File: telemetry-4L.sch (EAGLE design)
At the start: 65 parts, among them SW1 MF-SW-TACT-4.2MM, SW2 SWITCH_SPDT, U1 ATSAMD21G18A-MUT, U2 SPX3819M5-L-3-0, U3 MCP73831T-2ACI/OT, U4 DMG6968U, U5 SIM868, U6 BMP280, U7 MPU-9250, X1 S2B-PH-SM4-TB(LF)(SN)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

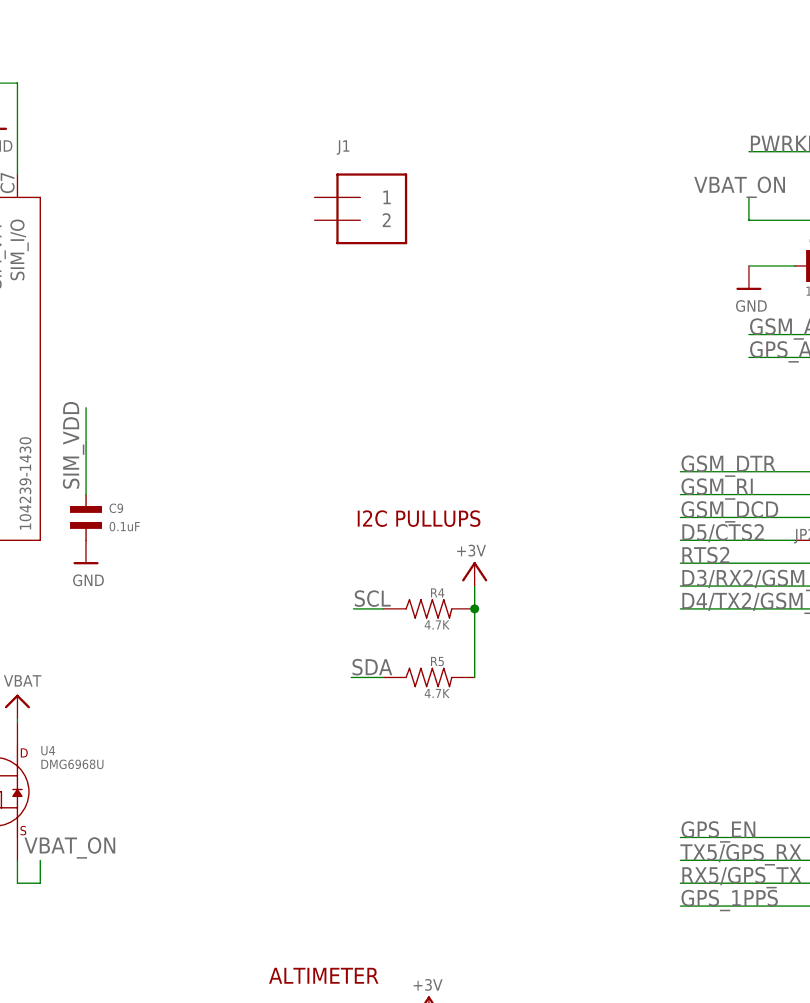
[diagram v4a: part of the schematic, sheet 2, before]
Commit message: Added a second JP2 socket for servo output
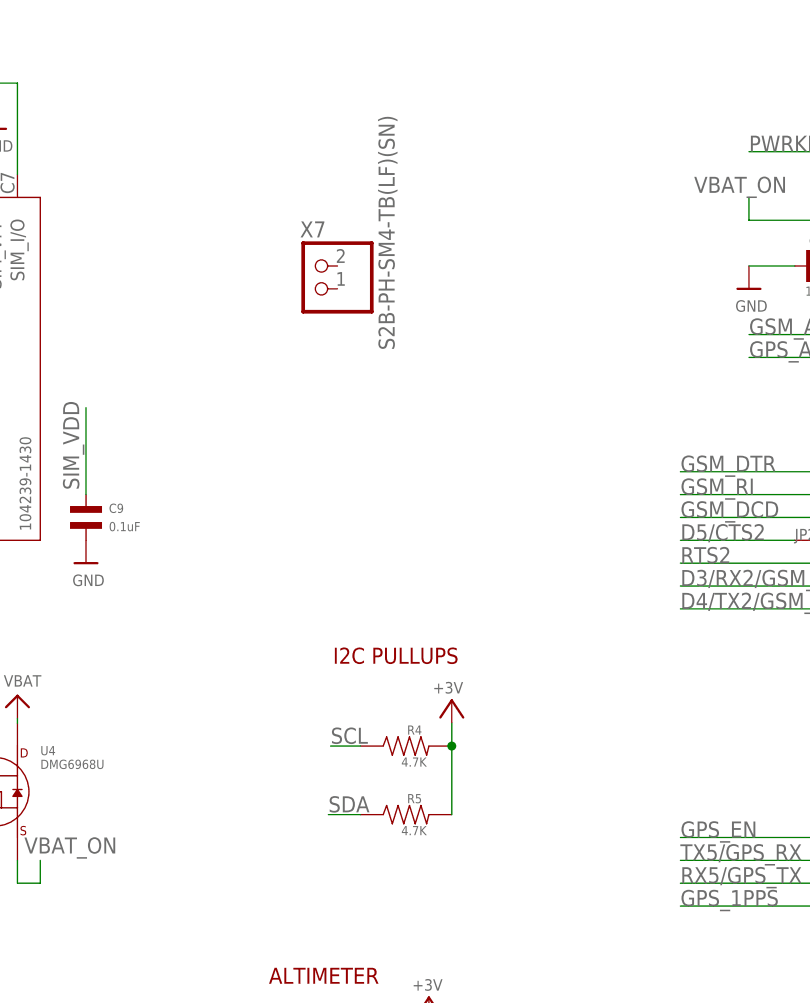
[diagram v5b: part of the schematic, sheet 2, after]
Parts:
- removed J1: (no value), microbuilder:TERMBLOCK_1X2
- added X7: S2B-PH-SM4-TB(LF)(SN), microbuilder:CON_JST_PH_2PIN
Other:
- moved on the sheet: R4, R5
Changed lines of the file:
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@@
 <part name="U$25" library="microbuilder" deviceset="GND" device=""/>
 <part name="U$26" library="microbuilder" deviceset="GND" device=""/>
-<part name="J1" library="microbuilder" deviceset="TERMBLOCK_1X2" device=""/>
+<part name="X7" library="microbuilder" deviceset="CON_JST_PH_2PIN" device="" value="S2B-PH-SM4-TB(LF)(SN)"/>
 </parts>
 <sheets>
@@
 <text x="96.52" y="65.024" size="1.778" layer="94">ALTIMETER</text>
 <text x="17.526" y="169.164" size="1.778" layer="94">SIM+SD COMBO SLOT</text>
-<text x="106.172" y="115.824" size="1.778" layer="94">I2C PULLUPS</text>
+<text x="103.632" y="100.584" size="1.778" layer="94">I2C PULLUPS</text>
 <text x="167.894" y="169.672" size="1.778" layer="94">GPS+GSM MODULE</text>
 <text x="131.572" y="44.196" size="1.778" layer="94">ANTENNAS</text>
@@
 <instance part="U5" gate="G$1" x="200.66" y="93.98"/>
 <instance part="U$37" gate="G$1" x="149.86" y="142.24"/>
-<instance part="+3V6" gate="G$1" x="119.38" y="111.76" smashed="yes" rot="MR0">
-<attribute name="VALUE" x="120.65" y="112.522" size="1.27" layer="96" rot="MR0"/>
+<instance part="+3V6" gate="G$1" x="116.84" y="96.52" smashed="yes" rot="MR0">
+<attribute name="VALUE" x="118.11" y="97.282" size="1.27" layer="96" rot="MR0"/>
 </instance>
 <instance part="X6" gate="G$1" x="149.86" y="22.86" smashed="yes">
@@
 <attribute name="VALUE" x="160.02" y="142.494" size="1.016" layer="96" font="vector" rot="R180"/>
 </instance>
-<instance part="R4" gate="G$1" x="114.3" y="106.68" smashed="yes" rot="R90">
-<attribute name="NAME" x="116.078" y="107.95" size="1.016" layer="95" font="vector" rot="R180" align="top-left"/>
-<attribute name="VALUE" x="116.586" y="105.41" size="1.016" layer="96" font="vector" rot="R180"/>
-</instance>
-<instance part="R5" gate="G$1" x="114.3" y="99.06" smashed="yes" rot="R90">
-<attribute name="NAME" x="116.078" y="100.33" size="1.016" layer="95" font="vector" rot="R180" align="top-left"/>
-<attribute name="VALUE" x="116.586" y="97.79" size="1.016" layer="96" font="vector" rot="R180"/>
+<instance part="R4" gate="G$1" x="111.76" y="91.44" smashed="yes" rot="R90">
+<attribute name="NAME" x="113.538" y="92.71" size="1.016" layer="95" font="vector" rot="R180" align="top-left"/>
+<attribute name="VALUE" x="114.046" y="90.17" size="1.016" layer="96" font="vector" rot="R180"/>
+</instance>
+<instance part="R5" gate="G$1" x="111.76" y="83.82" smashed="yes" rot="R90">
+<attribute name="NAME" x="113.538" y="85.09" size="1.016" layer="95" font="vector" rot="R180" align="top-left"/>
+<attribute name="VALUE" x="114.046" y="82.55" size="1.016" layer="96" font="vector" rot="R180"/>
 </instance>
 <instance part="C17" gate="G$1" x="7.62" y="88.9"/>
@@
 <instance part="U$25" gate="G$1" x="8.636" y="22.86"/>
 <instance part="U$26" gate="G$1" x="19.05" y="40.64"/>
-<instance part="J1" gate="G$1" x="106.68" y="149.86"/>
+<instance part="X7" gate="G$1" x="101.6" y="144.78" smashed="yes" rot="R180">
+<attribute name="NAME" x="102.87" y="149.733" size="1.778" layer="95" rot="R180"/>
+<attribute name="VALUE" x="108.712" y="161.544" size="1.778" layer="96" rot="R270"/>
+</instance>
 </instances>
 <busses>
@@
 <net name="SCL" class="0">
 <segment>
-<wire x1="105.918" y1="106.68" x2="109.22" y2="106.68" width="0.1524" layer="91"/>
-<label x="105.918" y="106.934" size="1.778" layer="95"/>
+<wire x1="103.378" y1="91.44" x2="106.68" y2="91.44" width="0.1524" layer="91"/>
+<label x="103.378" y="91.694" size="1.778" layer="95"/>
 <pinref part="R4" gate="G$1" pin="P$1"/>
 </segment>
@@
 <net name="SDA" class="0">
 <segment>
-<wire x1="105.664" y1="99.06" x2="109.22" y2="99.06" width="0.1524" layer="91"/>
-<label x="105.664" y="99.314" size="1.778" layer="95"/>
+<wire x1="103.124" y1="83.82" x2="106.68" y2="83.82" width="0.1524" layer="91"/>
+<label x="103.124" y="84.074" size="1.778" layer="95"/>
 <pinref part="R5" gate="G$1" pin="P$1"/>
 </segment>
@@
 <pinref part="R5" gate="G$1" pin="P$2"/>
 <pinref part="+3V6" gate="G$1" pin="+3V"/>
-<wire x1="119.38" y1="109.22" x2="119.38" y2="106.68" width="0.1524" layer="91"/>
+<wire x1="116.84" y1="93.98" x2="116.84" y2="91.44" width="0.1524" layer="91"/>
 <pinref part="R4" gate="G$1" pin="P$2"/>
-<wire x1="119.38" y1="106.68" x2="119.38" y2="99.06" width="0.1524" layer="91"/>
-<junction x="119.38" y="106.68"/>
-</segment>
-<segment>
+<wire x1="116.84" y1="91.44" x2="116.84" y2="83.82" width="0.1524" layer="91"/>
+<junction x="116.84" y="91.44"/>
+</segment>
+<segment>

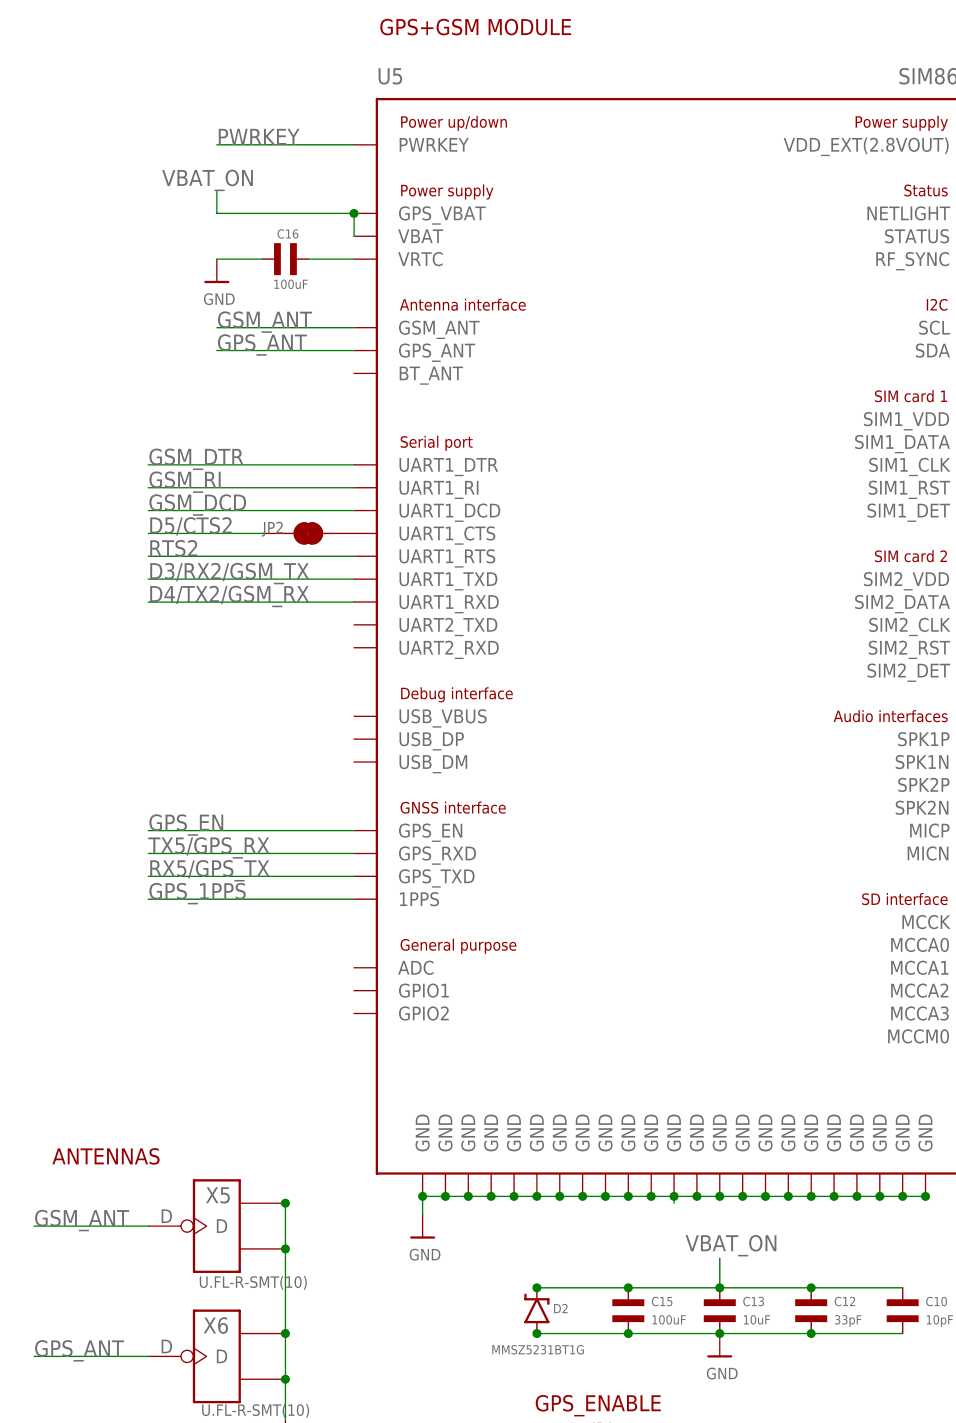
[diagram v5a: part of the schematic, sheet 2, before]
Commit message: Moved power mosfet out
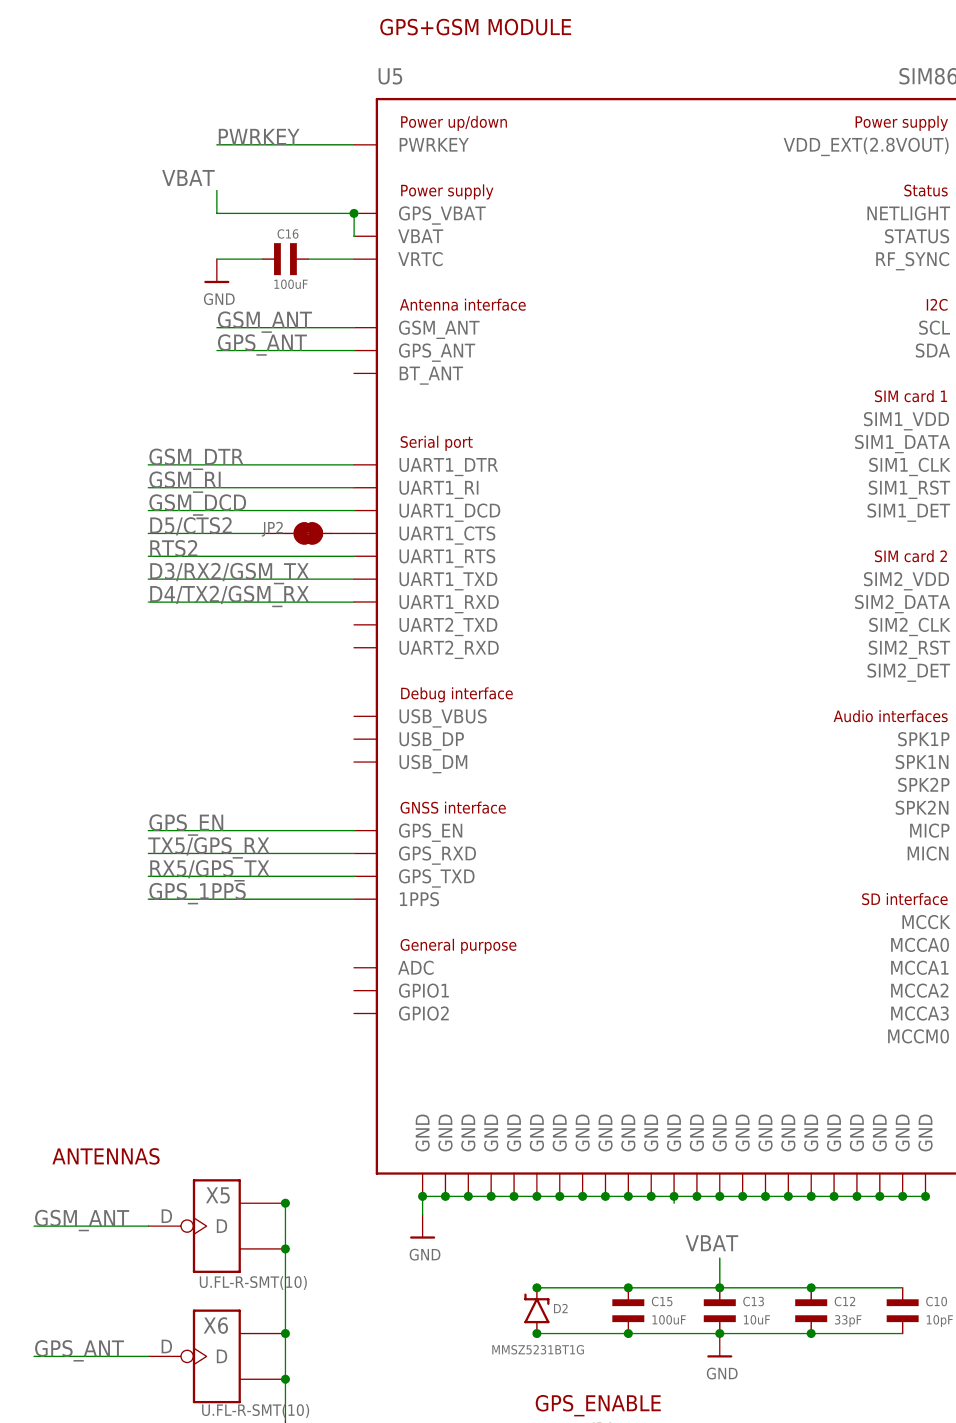
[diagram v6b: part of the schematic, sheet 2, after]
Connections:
- net VBAT: now also C10.P$1, C12.P$1, C13.P$1, C15.P$1, D2.C, R3.P$1, U5.GPS_VBAT, U5.VBAT
- net VBAT_ON: no longer C10.P$1, C12.P$1, C13.P$1, C15.P$1, D2.C, R3.P$1, U5.GPS_VBAT, U5.VBAT

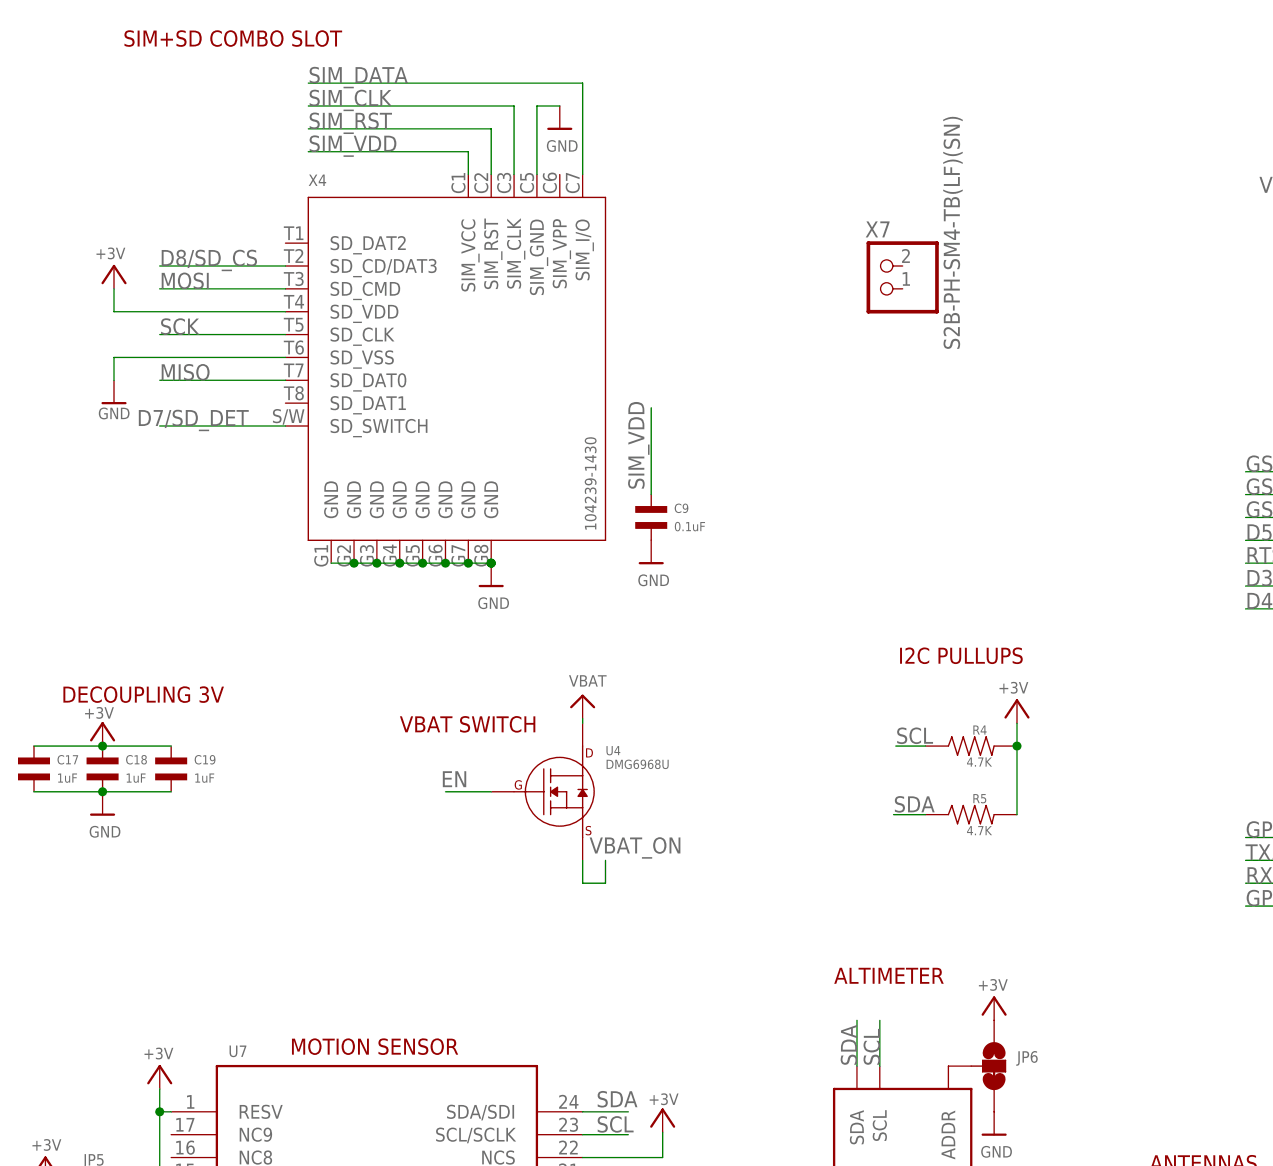
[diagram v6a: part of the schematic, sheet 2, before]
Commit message: Connected servo power in schematic
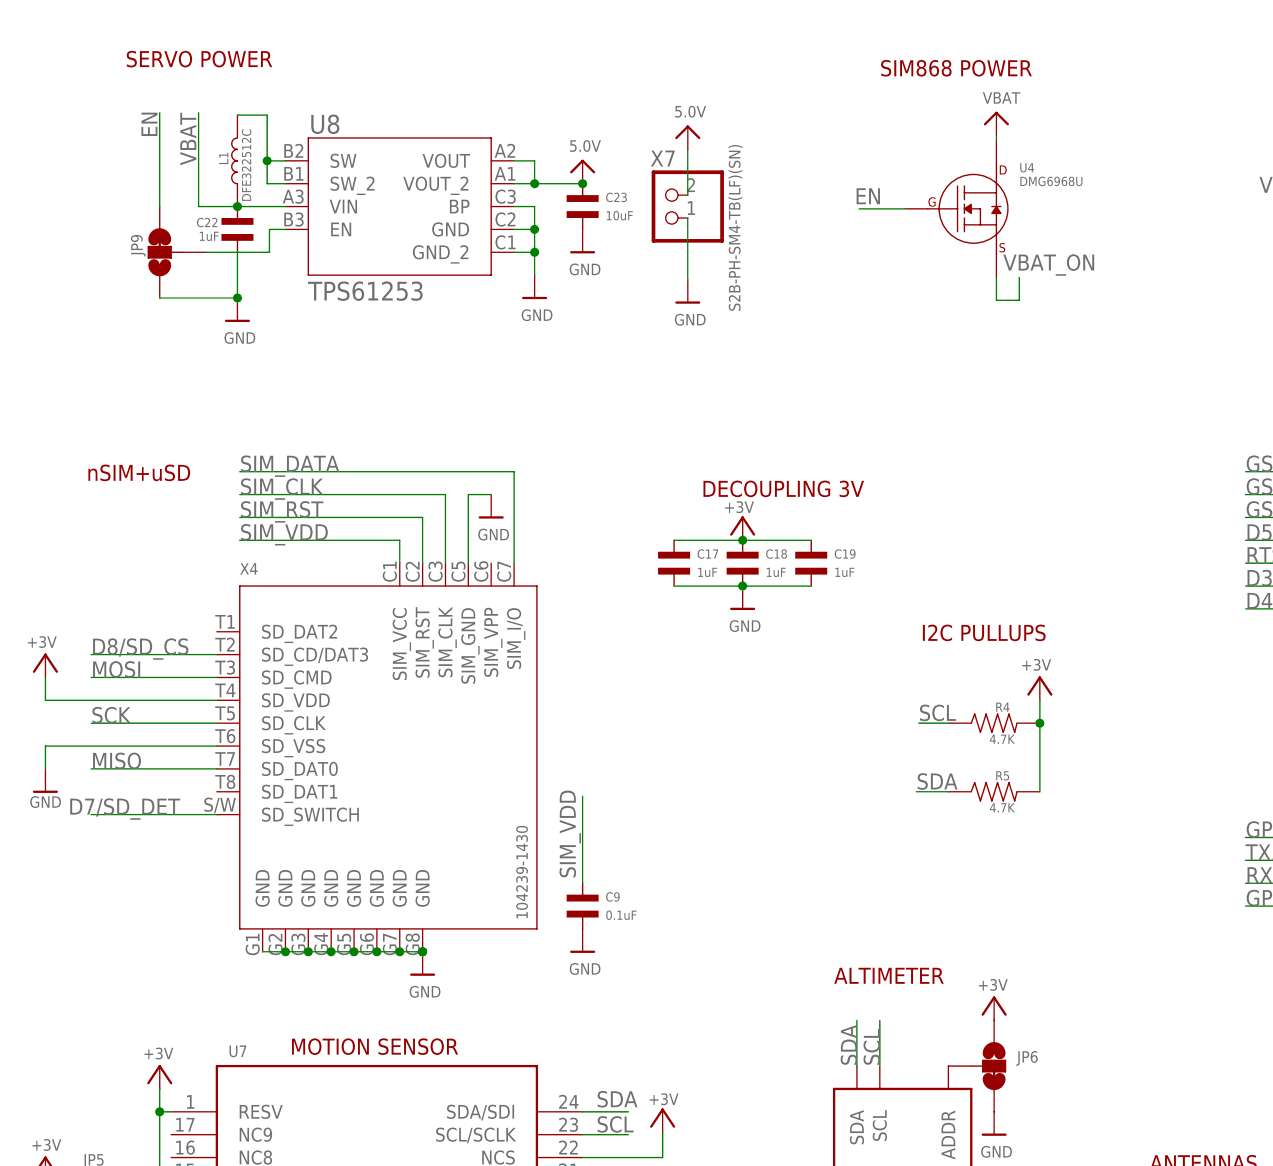
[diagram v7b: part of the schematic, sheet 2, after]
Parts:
- added C22: 1uF, MF_Passives:CAPACITOR_NP_0402
- added C23: 10uF, MF_Passives:CAPACITOR_NP_0603
- added JP9: JUMPER-PAD-3-2OF3_NC_BY_TRACE_SMALL, SparkFun-Passives:JUMPER-PAD-3-2OF3_NC_BY_TRACE_SMALL
- added L1: DFE322512C, MF_Passives:INDUCTOR_1210
- added U8: TPS61253, Custom:TPS61253YFFT
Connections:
- new net 5.0V: C23.P$1, U8.VOUT, U8.VOUT_2, X7.2
- new net N$14: JP9.2, U8.EN
- new net N$9: L1.P$2, U8.SW, U8.SW_2
- net EN: now also JP9.3
- net GND: now also C22.P$2, C23.P$2, JP9.1, U8.BP, U8.GND, U8.GND_2, X7.1
- net VBAT: now also C22.P$1, L1.P$1, U8.VIN
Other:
- note added: "SERVO POWER"
- note added: "SIM868 POWER"
- note added: "nSIM+uSD"
- note removed: "SIM+SD COMBO SLOT"
- note removed: "VBAT SWITCH"
- moved on the sheet: C17, C18, C19, C9, R4, R5, U4, X4, X7

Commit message: All done
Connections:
- net N$14 renamed 5V_EN
- net VBAT: no longer C10.P$1, C12.P$1, C13.P$1, C15.P$1, D2.C, U5.GPS_VBAT, U5.VBAT
- net VBAT_ON: now also C10.P$1, C12.P$1, C13.P$1, C15.P$1, D2.C, U5.GPS_VBAT, U5.VBAT
